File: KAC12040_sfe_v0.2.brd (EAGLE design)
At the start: 101.6 x 57.1 mm, 9 parts

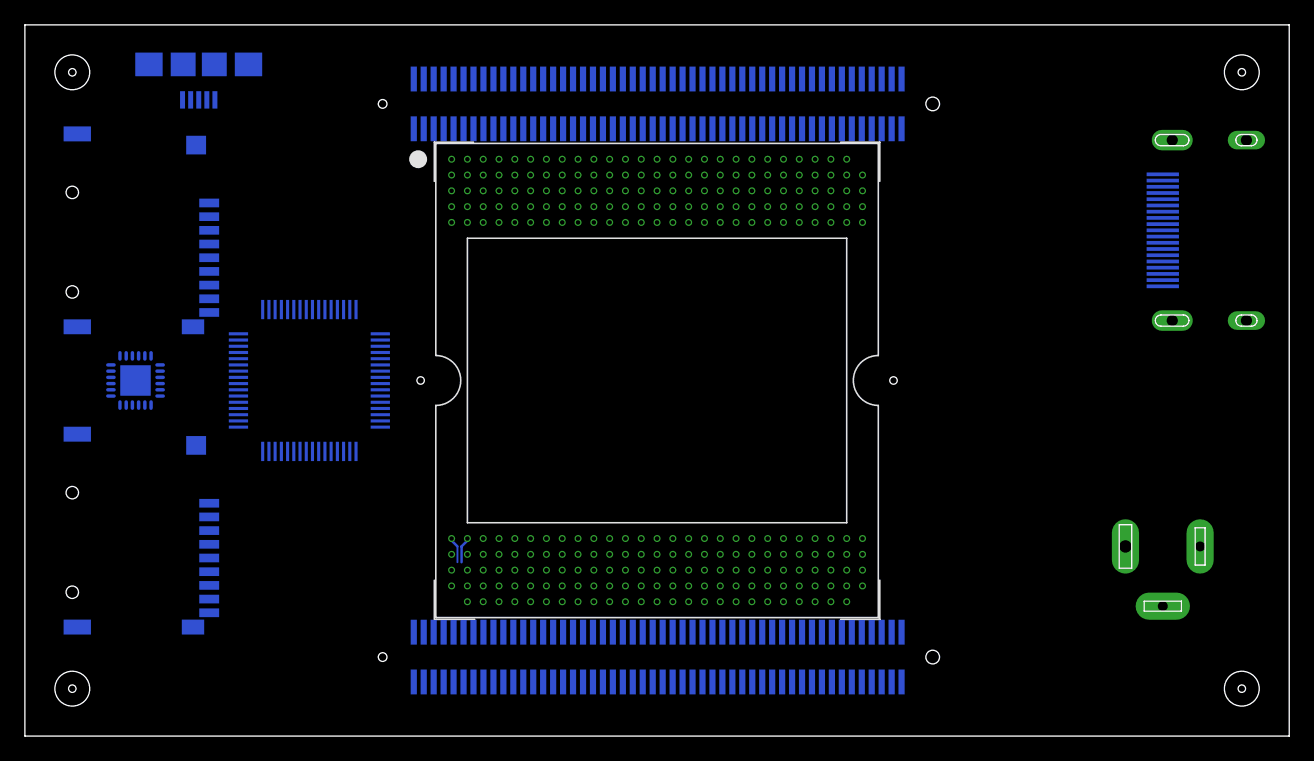
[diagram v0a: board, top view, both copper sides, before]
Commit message: Minor library changes and part placement
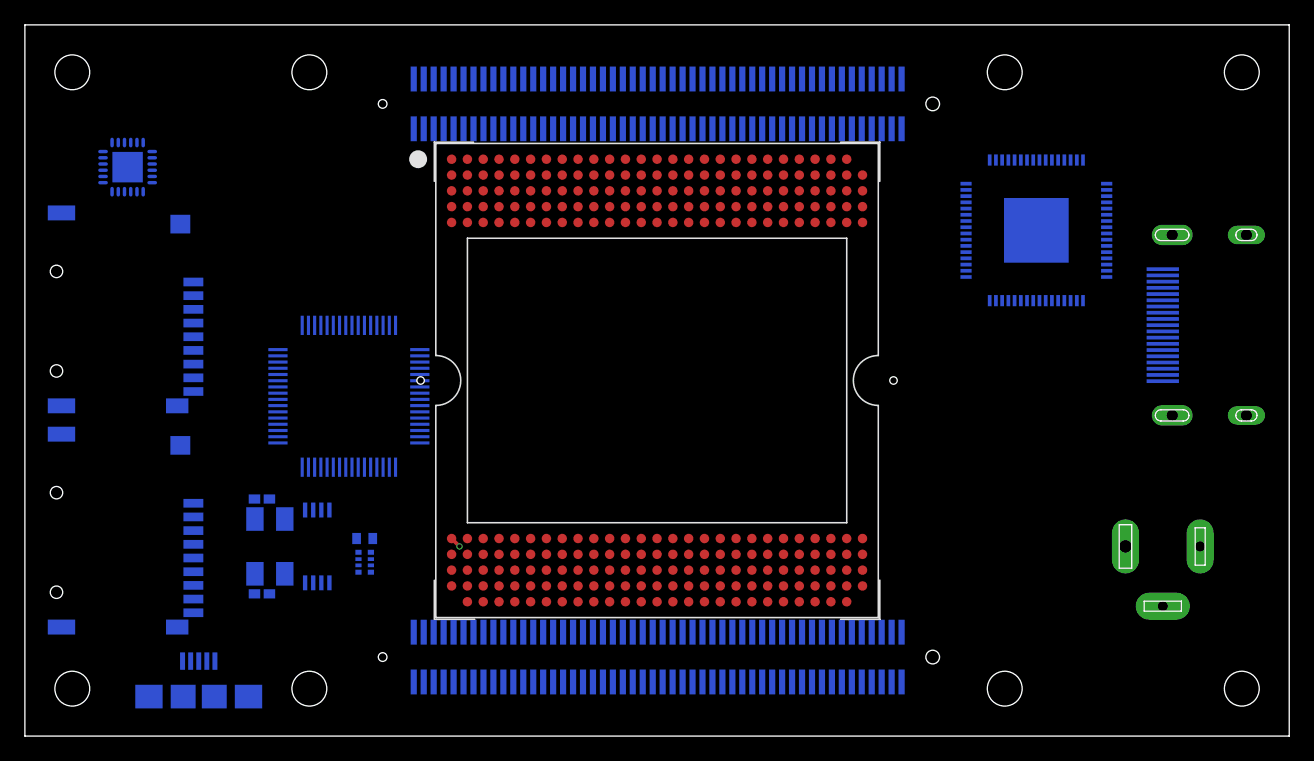
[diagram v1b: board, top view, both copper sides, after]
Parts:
- removed U$2, U$3: MICRO-SD3, micro-sd:TF-MICRO-SD_PP3
- added C1, C2: (no value), rcl:C0402K
- added IC2: 93LC46ST, microchip:TSSOP8
- added Q1: (no value), crystal:CTS406
- added R1: (no value), rcl:R0402
- added RN1: (no value), resistor-dil:4X0402ARV341
- added U$5: ADV7513, adv7513:LQFP-ST-64-2
- added µSD0, µSD1: MICRO-SD3, micro-sd:TF-MICRO-SD_PP3
- U$1: value KAC-12040 -> KAC-12040-RB501T4; device KAC-12040:KAC-12040-400T4 -> KAC-12040:KAC-12040-RB501T4
- moved U1 50.8 mm to (14.0, 3.17), turned to 90 degrees
- moved U$4 17.2 mm to (8.26, 45.7), turned to 270 degrees
- moved CN1 7.62 mm to (91.4, 33.0)
- moved U2 3.42 mm to (26.0, 27.3), turned to 180 degrees
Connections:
- removed net VCC_A: U$4.P$5
- removed net VCC_B0: U$4.P$21
- removed net VCC_B1: U$4.P$17
- new net AVDD: U$5.15, U$5.19, U$5.25
- new net A_VCC: U$4.5
- new net B0_CLK: U$4.19, µSD0.5
- new net B0_CMD: U$4.20, µSD0.3
- new net B0_DAT0: U$4.18, µSD0.7
- new net B0_DAT1: U$4.16, µSD0.8
- new net B0_DAT2: U$4.23, µSD0.1
- new net B0_DAT3: U$4.22, µSD0.2
- new net B0_VCC: U$4.21
- new net B1_CLK: U$4.13, µSD1.5
- new net B1_CMD: U$4.12, µSD1.3
- new net B1_DAT0: U$4.14, µSD1.7
- new net B1_DAT1: U$4.15, µSD1.8
- new net B1_DAT2: U$4.8, µSD1.1
- new net B1_DAT3: U$4.10, µSD1.2
- new net B1_VCC: U$4.17
- new net BGVDD: U$5.13
- new net DVDD: U$5.1, U$5.11, U$5.31, U$5.51
- new net DVDD_3V: U$5.29
- new net EE_CLK: IC2.2, RN1.2, U2.62
- new net EE_CS: IC2.1, RN1.1, U2.63
- new net EE_DATA: IC2.3, R1.2, U2.61
- new net EPAD: U$5.EPAD
- new net N$10: U1.D+, U2.8
- new net N$11: IC2.4, R1.1, RN1.3
- new net N$12: IC2.6, IC2.8, RN1.6, RN1.7, RN1.8
- new net N$13: U2.38, ZED1.1
- new net N$14: C1.1, Q1.3, U2.2
- new net N$15: C2.1, Q1.1, U2.3
- new net N$16: U2.39, ZED1.4
- new net N$17: U2.40, ZED1.3
- new net N$18: U2.41, ZED1.2
- new net N$19: U2.20, U2.31, U2.42, U2.56
- new net N$20: U2.12, U2.37, U2.64
- new net N$21: ZED1.187
- new net N$22: ZED1.174
- new net N$23: ZED1.124
- new net N$24: ZED1.81
- new net N$25: ZED1.68
- new net N$26: ZED1.18
- new net N$5: µSD0.4
- new net N$6: µSD0.6
- new net N$7: µSD1.6
- new net N$8: µSD1.4
- new net N$9: U1.D-, U2.7
- new net PVDD: U$5.12
- net ECPAD: now also U$4.EPAD; no longer U$4.P$25
- net GND: now also C1.2, C2.2, IC2.5, U$4.11, U$4.2, U2.1, U2.11, U2.15, U2.25, U2.35, U2.47, U2.5, U2.51; no longer U$4.P$11, U$4.P$2
- net MT: now also µSD0.MT1, µSD0.MT2, µSD0.MT3, µSD0.MT4, µSD1.MT1, µSD1.MT2, µSD1.MT3, µSD1.MT4; no longer U$2.MT1, U$2.MT2, U$2.MT3, U$2.MT4, U$3.MT1, U$3.MT2, U$3.MT3, U$3.MT4
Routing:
- net C$0_N: track 2.10 -> 0.00 mm
- net C$0_P: track 2.10 -> 3.44 mm, vias 0 -> 1

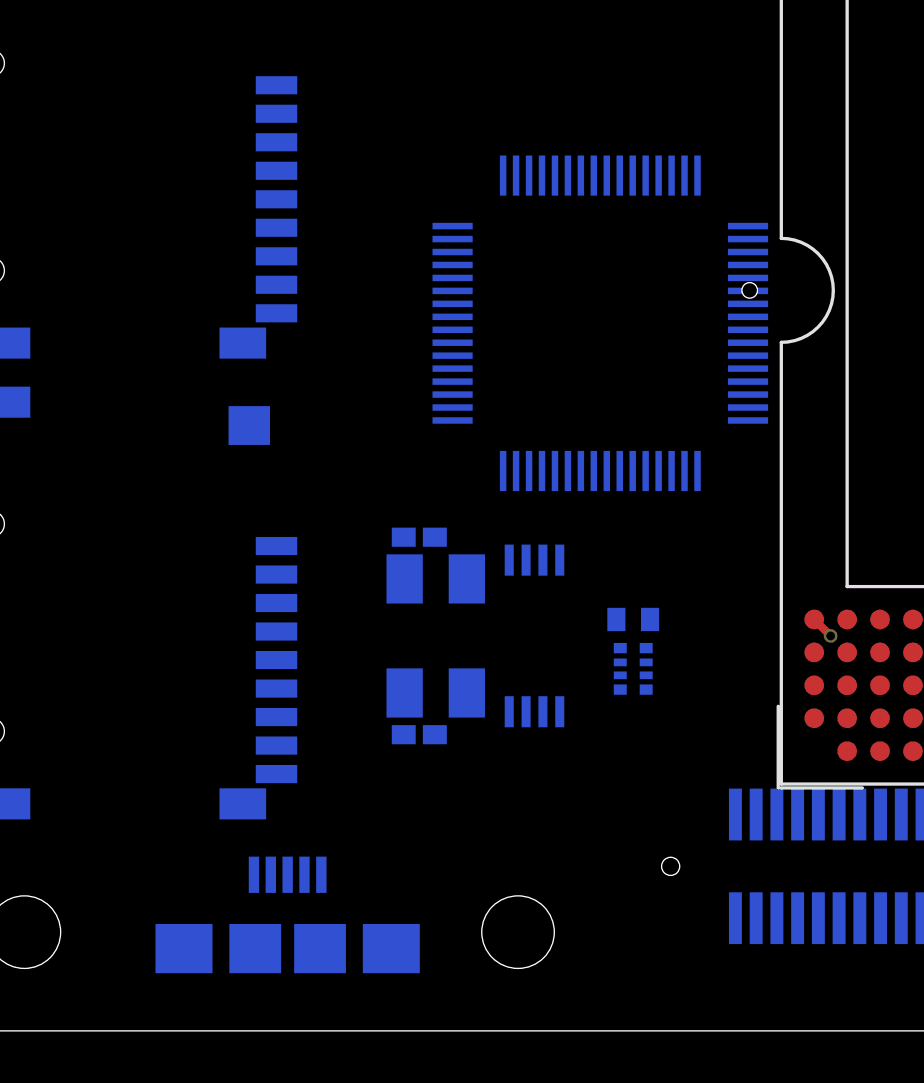
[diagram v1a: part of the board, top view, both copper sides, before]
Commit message: Another update to the design
 - Replaced FT2232H with FT232H (single channel)
 - Added SD PMOD interface
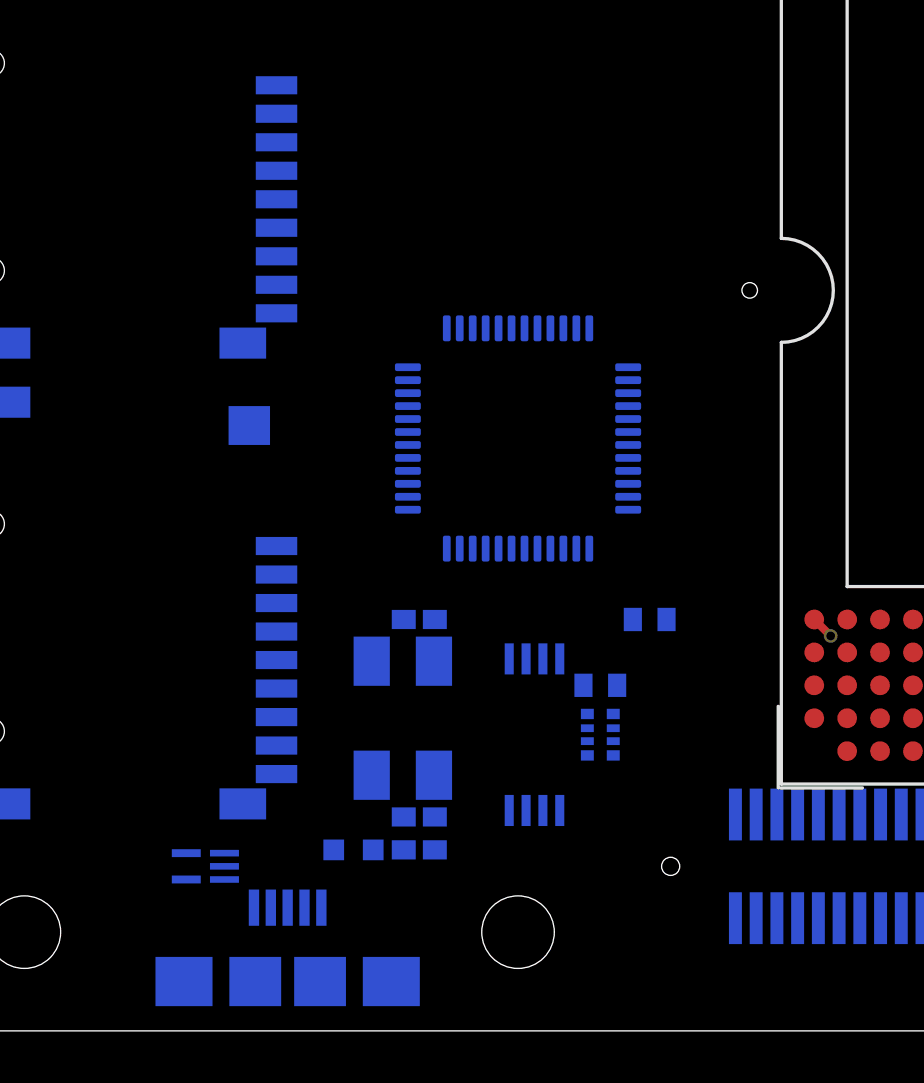
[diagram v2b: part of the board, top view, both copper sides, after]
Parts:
- added C3: 100n, rcl:C0402K
- added FB1: 600R, microbuilder:_0603MP
- added R2: 12k, rcl:R0402
- added U$2: FT232H, ft232h:LQFP48
- R1: value (none) -> 2k
- U2: value (none) -> TPD3E001DRLR; device microbuilder:LQFP64 -> esd:SOT50P160X60-5N
- moved U2 25.9 mm to (10.8, 6.35), turned to 0 degrees
- moved C1 10.8 mm to (19.1, 8.26), turned to 180 degrees
- moved C2 4.45 mm to (19.1, 15.9), turned to 0 degrees
- moved IC2 3.81 mm to (23.5, 11.4)
- moved Q1 3.42 mm to (18.4, 12.1), turned to 270 degrees
- moved RN1 2.84 mm to (26.0, 11.4)
- moved R1 2.84 mm to (26.0, 13.3)
- moved U1 1.27 mm to (14.0, 1.91)
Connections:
- new net A_CLK: U$4.9, ZED1.104
- new net A_CMD: U$4.4, ZED1.103
- new net A_DAT0: U$4.6, ZED1.102
- new net A_DAT1: U$4.7, ZED1.101
- new net A_DAT2: U$4.1, ZED1.107
- new net A_DAT3: U$4.3, ZED1.108
- new net N$27: RN1.4, U$2.34
- new net N$28: U$2.7, U1.D+, U2.2
- new net N$29: U$2.6, U1.D-, U2.1
- new net N$30: U$4.11, U$4.2
- new net N$32: R2.2, U$2.5
- new net SEL: U$4.24, ZED1.105
- new net VCCD: U$2.39
- new net VPHY: U$2.3
- new net VPLL: U$2.8
- net EE_CLK: now also U$2.44; no longer U2.62
- net EE_CS: now also U$2.45; no longer U2.63
- net EE_DATA: now also U$2.43; no longer U2.61
- net GND: now also C3.2, R2.1, U$2.10, U$2.11, U$2.22, U$2.23, U$2.35, U$2.36, U$2.4, U$2.41, U$2.47, U$2.48, U$2.9, U1.GND, U2.3; no longer U$4.11, U$4.2, U2.1, U2.11, U2.15, U2.25, U2.35, U2.47, U2.5, U2.51
- net N$10: now also C3.1, FB1.1, U1.VBUS, U2.5; no longer U1.D+, U2.8
- net N$13: now also U$2.13; no longer U2.38
- net N$14: now also U$2.1; no longer U2.2
- net N$15: now also U$2.2; no longer U2.3
- net N$16: now also U$2.14; no longer U2.39
- net N$17: now also U$2.15; no longer U2.40
- net N$18: now also U$2.16; no longer U2.41
- net N$19: now also U$2.12, U$2.24, U$2.46; no longer U2.20, U2.31, U2.42, U2.56
- net N$20: now also U1.ID, U2.4; no longer U2.12, U2.37, U2.64
- net N$9: now also FB1.2, U$2.40; no longer U1.D-, U2.7
